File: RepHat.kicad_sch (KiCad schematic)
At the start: 8 parts, among them J1 GPIO, J12 Conn_01x03_Pin, J13 Conn_01x03_Pin, J14 Conn_01x03_Pin, J15 Conn_01x03_Pin, J16 Conn_01x03_Pin, J17 Screw_Terminal_01x02, J2 Screw_Terminal_01x02

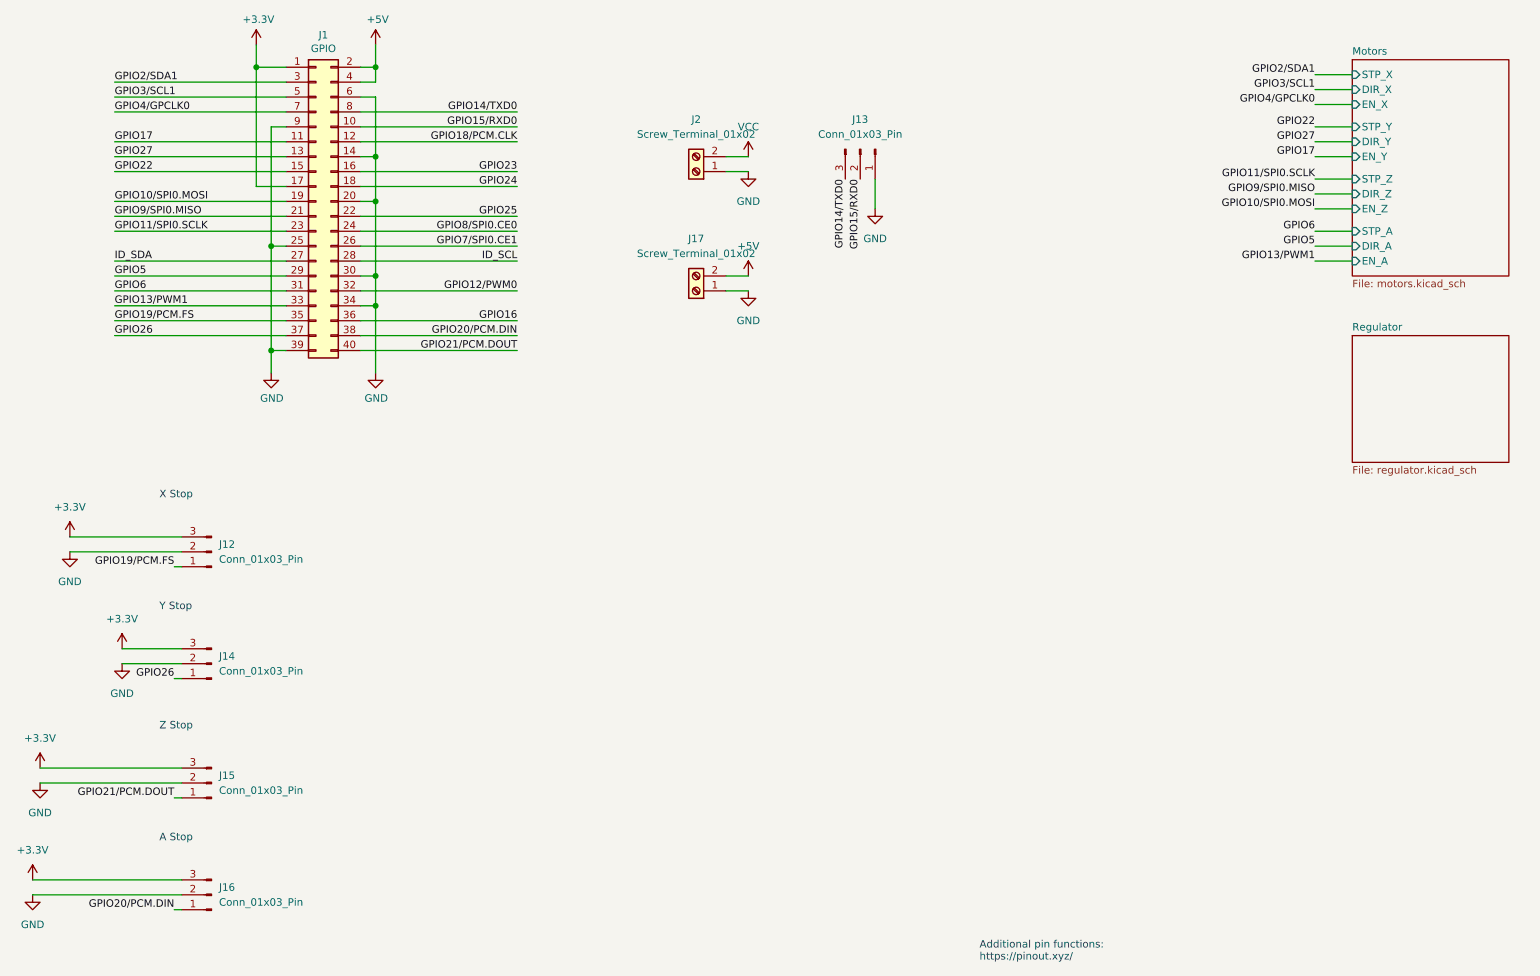
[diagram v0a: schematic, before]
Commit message: Endstops buffered & regulator 1MHz
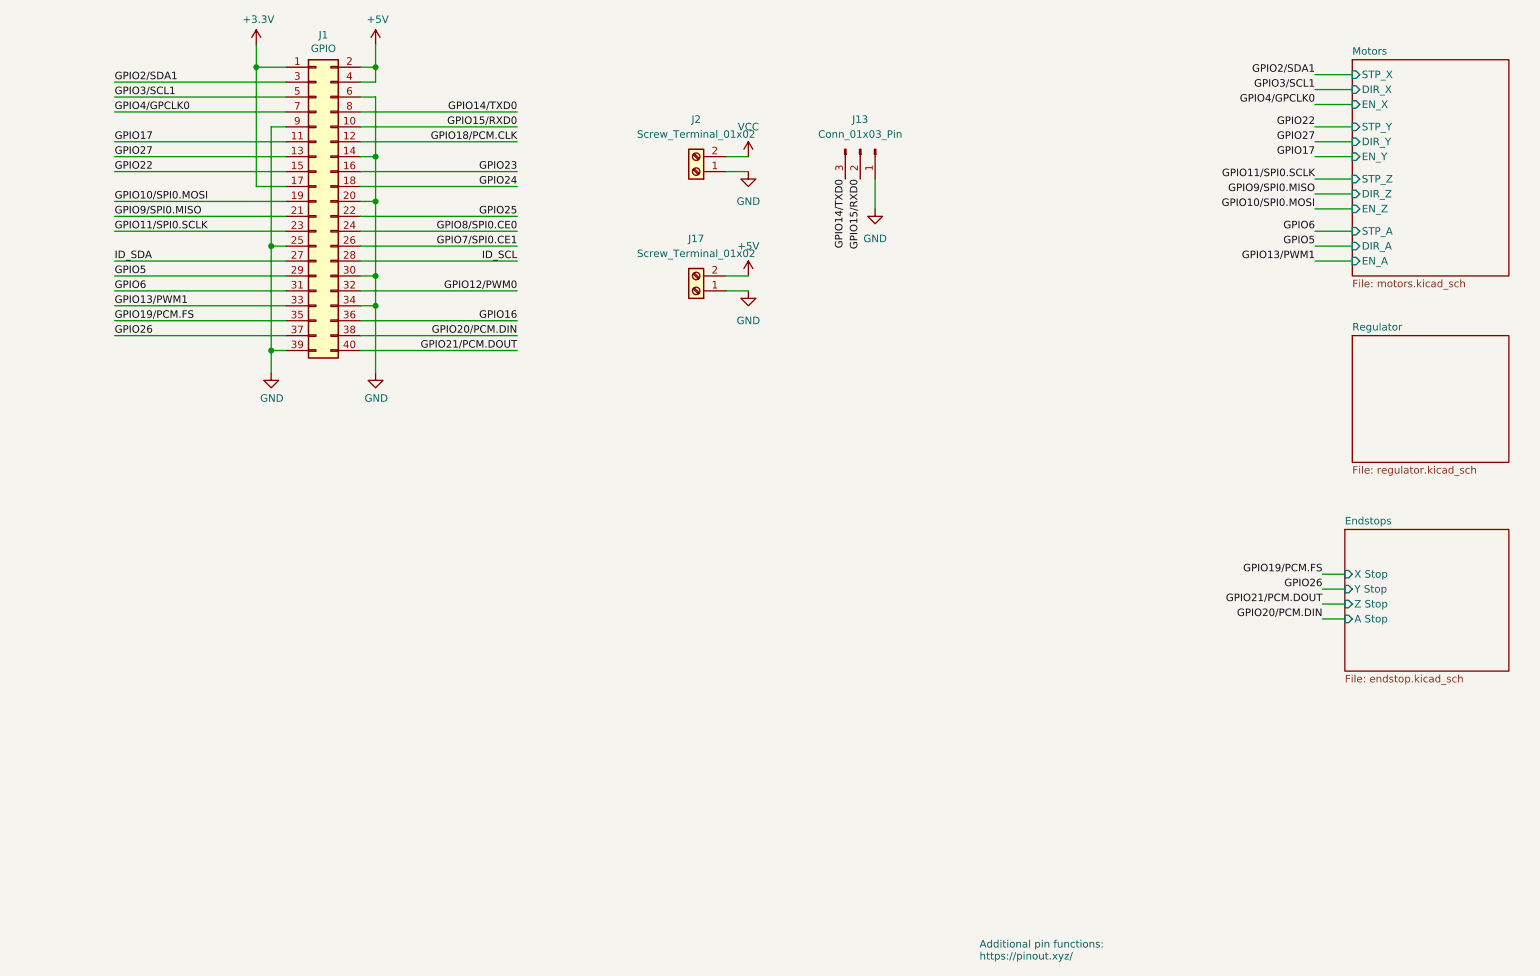
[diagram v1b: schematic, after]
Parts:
- removed J12, J14, J15, J16: Conn_01x03_Pin, Connector_JST:JST_XH_B3B-XH-A_1x03_P2.50mm_Vertical, symbol Connector:Conn_01x03_Pin
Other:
- added sheet Endstops (endstop.kicad_sch)
- note removed: "A Stop"
- note removed: "X Stop"
- note removed: "Y Stop"
- note removed: "Z Stop"
